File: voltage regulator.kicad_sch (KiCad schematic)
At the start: 9 parts, among them U1 AP63200WU-7

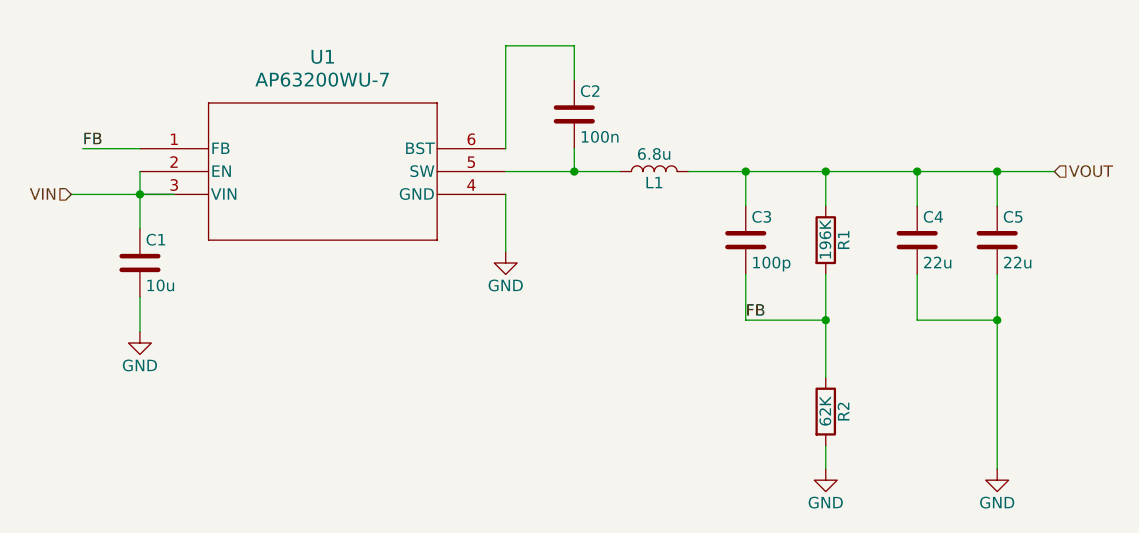
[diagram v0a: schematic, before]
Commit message: Add oscillator, mounting holes, switches
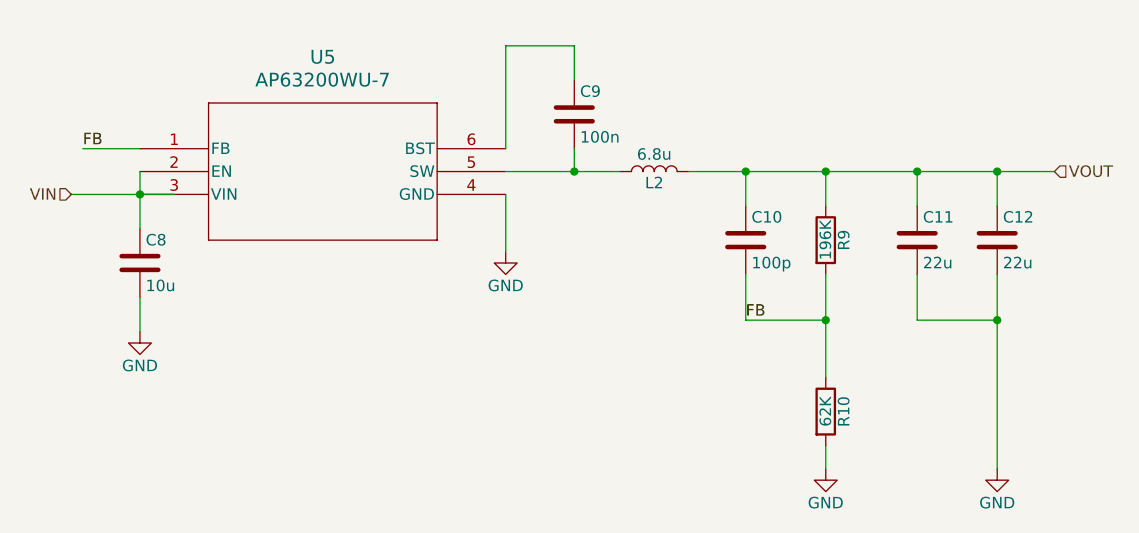
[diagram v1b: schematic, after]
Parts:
- C10: renamed from C3; footprint (none) -> Capacitor_SMD:C_0201_0603Metric_Pad0.64x0.40mm_HandSolder
- C11: renamed from C4; footprint (none) -> Capacitor_SMD:C_0201_0603Metric_Pad0.64x0.40mm_HandSolder
- C12: renamed from C5; footprint (none) -> Capacitor_SMD:C_0201_0603Metric_Pad0.64x0.40mm_HandSolder
- C8: renamed from C1; footprint (none) -> Capacitor_SMD:C_0201_0603Metric_Pad0.64x0.40mm_HandSolder
- C9: renamed from C2; footprint (none) -> Capacitor_SMD:C_0201_0603Metric_Pad0.64x0.40mm_HandSolder
- L2: renamed from L1; footprint (none) -> Inductor_SMD:L_0603_1608Metric_Pad1.05x0.95mm_HandSolder
- R10: renamed from R2; footprint (none) -> Resistor_SMD:R_0603_1608Metric_Pad0.98x0.95mm_HandSolder
- R9: renamed from R1; footprint (none) -> Resistor_SMD:R_0603_1608Metric_Pad0.98x0.95mm_HandSolder
- renumbered U1 to U5
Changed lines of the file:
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@@
 		(on_board yes)
 		(dnp no)
-		(property "Reference" "C1"
+		(property "Reference" "C8"
 			(at 100.965 95.25 0)
 			(effects
@@
 			)
 		)
-		(property "Footprint" ""
+		(property "Footprint" "Capacitor_SMD:C_0201_0603Metric_Pad0.64x0.40mm_HandSolder"
 			(at 101.2952 101.6 0)
 			(effects
@@
 		(instances
 			(project "pitch shifter"
-				(path "/155ecfb0-8543-4b20-91a8-ba83977b0554/d343d846-0f09-4042-8be7-83c2141e6a90"
-					(reference "C1")
+				(path "/155ecfb0-8543-4b20-91a8-ba83977b0554/04f7cbcd-02ba-401a-9ce7-de3392119ba4"
+					(reference "C8")
 					(unit 1)
 				)
@@
 		(on_board yes)
 		(dnp no)
-		(property "Reference" "U1"
+		(property "Reference" "U5"
 			(at 120.65 74.93 0)
 			(effects
@@
 		)
 		(instances
-			(project ""
-				(path "/155ecfb0-8543-4b20-91a8-ba83977b0554/d343d846-0f09-4042-8be7-83c2141e6a90"
-					(reference "U1")
+			(project "pitch shifter"
+				(path "/155ecfb0-8543-4b20-91a8-ba83977b0554/04f7cbcd-02ba-401a-9ce7-de3392119ba4"
+					(reference "U5")
 					(unit 1)
 				)
@@
 		(on_board yes)
 		(dnp no)
-		(property "Reference" "#PWR?"
+		(property "Reference" "#PWR014"
 			(at 195.58 127 0)
 			(effects
@@
 		(instances
 			(project "pitch shifter"
-				(path "/155ecfb0-8543-4b20-91a8-ba83977b0554/d343d846-0f09-4042-8be7-83c2141e6a90"
-					(reference "#PWR?")
+				(path "/155ecfb0-8543-4b20-91a8-ba83977b0554/04f7cbcd-02ba-401a-9ce7-de3392119ba4"
+					(reference "#PWR014")
 					(unit 1)
 				)
@@
 		(on_board yes)
 		(dnp no)
-		(property "Reference" "C3"
+		(property "Reference" "C10"
 			(at 168.275 92.71 0)
 			(effects
@@
 			)
 		)
-		(property "Footprint" ""
+		(property "Footprint" "Capacitor_SMD:C_0201_0603Metric_Pad0.64x0.40mm_HandSolder"
 			(at 168.6052 99.06 0)
 			(effects
@@
 		(instances
 			(project "pitch shifter"
-				(path "/155ecfb0-8543-4b20-91a8-ba83977b0554/d343d846-0f09-4042-8be7-83c2141e6a90"
-					(reference "C3")
+				(path "/155ecfb0-8543-4b20-91a8-ba83977b0554/04f7cbcd-02ba-401a-9ce7-de3392119ba4"
+					(reference "C10")
 					(unit 1)
 				)
@@
 		(on_board yes)
 		(dnp no)
-		(property "Reference" "#PWR?"
+		(property "Reference" "#PWR011"
 			(at 100.33 111.76 0)
 			(effects
@@
 		(instances
 			(project "pitch shifter"
-				(path "/155ecfb0-8543-4b20-91a8-ba83977b0554/d343d846-0f09-4042-8be7-83c2141e6a90"
-					(reference "#PWR?")
+				(path "/155ecfb0-8543-4b20-91a8-ba83977b0554/04f7cbcd-02ba-401a-9ce7-de3392119ba4"
+					(reference "#PWR011")
 					(unit 1)
 				)
@@
 		(on_board yes)
 		(dnp no)
-		(property "Reference" "C5"
+		(property "Reference" "C12"
 			(at 196.215 92.71 0)
 			(effects
@@
 			)
 		)
-		(property "Footprint" ""
+		(property "Footprint" "Capacitor_SMD:C_0201_0603Metric_Pad0.64x0.40mm_HandSolder"
 			(at 196.5452 99.06 0)
 			(effects
@@
 		(instances
 			(project "pitch shifter"
-				(path "/155ecfb0-8543-4b20-91a8-ba83977b0554/d343d846-0f09-4042-8be7-83c2141e6a90"
-					(reference "C5")
+				(path "/155ecfb0-8543-4b20-91a8-ba83977b0554/04f7cbcd-02ba-401a-9ce7-de3392119ba4"
+					(reference "C12")
 					(unit 1)
 				)
@@
 		(on_board yes)
 		(dnp no)
-		(property "Reference" "R1"
+		(property "Reference" "R9"
 			(at 178.562 95.25 90)
 			(effects
@@
 			)
 		)
-		(property "Footprint" ""
+		(property "Footprint" "Resistor_SMD:R_0603_1608Metric_Pad0.98x0.95mm_HandSolder"
 			(at 174.752 95.25 90)
 			(effects
@@
 		)
 		(instances
-			(project ""
-				(path "/155ecfb0-8543-4b20-91a8-ba83977b0554/d343d846-0f09-4042-8be7-83c2141e6a90"
-					(reference "R1")
+			(project "pitch shifter"
+				(path "/155ecfb0-8543-4b20-91a8-ba83977b0554/04f7cbcd-02ba-401a-9ce7-de3392119ba4"
+					(reference "R9")
 					(unit 1)
 				)
@@
 		(on_board yes)
 		(dnp no)
-		(property "Reference" "L1"
+		(property "Reference" "L2"
 			(at 157.48 88.9 90)
 			(effects
@@
 			)
 		)
-		(property "Footprint" ""
+		(property "Footprint" "Inductor_SMD:L_0603_1608Metric_Pad1.05x0.95mm_HandSolder"
 			(at 157.48 87.63 0)
 			(effects
@@
 		)
 		(instances
-			(project ""
-				(path "/155ecfb0-8543-4b20-91a8-ba83977b0554/d343d846-0f09-4042-8be7-83c2141e6a90"
-					(reference "L1")
+			(project "pitch shifter"
+				(path "/155ecfb0-8543-4b20-91a8-ba83977b0554/04f7cbcd-02ba-401a-9ce7-de3392119ba4"
+					(reference "L2")
 					(unit 1)
 				)
@@
 		(on_board yes)
 		(dnp no)
-		(property "Reference" "R2"
+		(property "Reference" "R10"
 			(at 178.562 114.3 90)
 			(effects
@@
 			)
 		)
-		(property "Footprint" ""
+		(property "Footprint" "Resistor_SMD:R_0603_1608Metric_Pad0.98x0.95mm_HandSolder"
 			(at 174.752 114.3 90)
 			(effects
@@
 		(instances
 			(project "pitch shifter"
-				(path "/155ecfb0-8543-4b20-91a8-ba83977b0554/d343d846-0f09-4042-8be7-83c2141e6a90"
-					(reference "R2")
+				(path "/155ecfb0-8543-4b20-91a8-ba83977b0554/04f7cbcd-02ba-401a-9ce7-de3392119ba4"
+					(reference "R10")
 					(unit 1)
 				)
@@
 		(on_board yes)
 		(dnp no)
-		(property "Reference" "C2"
+		(property "Reference" "C9"
 			(at 149.225 78.74 0)
 			(effects
@@
 			)
 		)
-		(property "Footprint" ""
+		(property "Footprint" "Capacitor_SMD:C_0201_0603Metric_Pad0.64x0.40mm_HandSolder"
 			(at 149.5552 85.09 0)
 			(effects
@@
 		)
 		(instances
-			(project ""
-				(path "/155ecfb0-8543-4b20-91a8-ba83977b0554/d343d846-0f09-4042-8be7-83c2141e6a90"
-					(reference "C2")
+			(project "pitch shifter"
+				(path "/155ecfb0-8543-4b20-91a8-ba83977b0554/04f7cbcd-02ba-401a-9ce7-de3392119ba4"
+					(reference "C9")
 					(unit 1)
 				)
@@
 		(on_board yes)
 		(dnp no)
-		(property "Reference" "C4"
+		(property "Reference" "C11"
 			(at 187.325 92.71 0)
 			(effects
@@
 			)
 		)
-		(property "Footprint" ""
+		(property "Footprint" "Capacitor_SMD:C_0201_0603Metric_Pad0.64x0.40mm_HandSolder"
 			(at 187.6552 99.06 0)
 			(effects
@@
 		(instances
 			(project "pitch shifter"
-				(path "/155ecfb0-8543-4b20-91a8-ba83977b0554/d343d846-0f09-4042-8be7-83c2141e6a90"
-					(reference "C4")
+				(path "/155ecfb0-8543-4b20-91a8-ba83977b0554/04f7cbcd-02ba-401a-9ce7-de3392119ba4"
+					(reference "C11")
 					(unit 1)
 				)
@@
 		(on_board yes)
 		(dnp no)
-		(property "Reference" "#PWR?"
+		(property "Reference" "#PWR013"
 			(at 176.53 127 0)
 			(effects
@@
 		(instances
 			(project "pitch shifter"
-				(path "/155ecfb0-8543-4b20-91a8-ba83977b0554/d343d846-0f09-4042-8be7-83c2141e6a90"
-					(reference "#PWR?")
+				(path "/155ecfb0-8543-4b20-91a8-ba83977b0554/04f7cbcd-02ba-401a-9ce7-de3392119ba4"
+					(reference "#PWR013")
 					(unit 1)
 				)
@@
 		(on_board yes)
 		(dnp no)
-		(property "Reference" "#PWR?"
+		(property "Reference" "#PWR012"
 			(at 140.97 102.87 0)
 			(effects
@@
 		)
 		(instances
-			(project ""
-				(path "/155ecfb0-8543-4b20-91a8-ba83977b0554/d343d846-0f09-4042-8be7-83c2141e6a90"
-					(reference "#PWR?")
-					(unit 1)
-				)
+			(project "pitch shifter"
+				(path "/155ecfb0-8543-4b20-91a8-ba83977b0554/04f7cbcd-02ba-401a-9ce7-de3392119ba4"
+					(reference "#PWR012")
+					(unit 1)
+				)

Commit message: Began board layout
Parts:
- removed C10: 100p, Capacitor_SMD:C_0201_0603Metric_Pad0.64x0.40mm_HandSolder, symbol Device:C
- removed C11, C12: 22u, Capacitor_SMD:C_0201_0603Metric_Pad0.64x0.40mm_HandSolder, symbol Device:C
- removed C8: 10u, Capacitor_SMD:C_0201_0603Metric_Pad0.64x0.40mm_HandSolder, symbol Device:C
- removed C9: 100n, Capacitor_SMD:C_0201_0603Metric_Pad0.64x0.40mm_HandSolder, symbol Device:C
- removed R10: 62K, Resistor_SMD:R_0603_1608Metric_Pad0.98x0.95mm_HandSolder, symbol Device:R
- removed R9: 196K, Resistor_SMD:R_0603_1608Metric_Pad0.98x0.95mm_HandSolder, symbol Device:R
- added C15: 10u, Capacitor_SMD:C_0603_1608Metric_Pad1.08x0.95mm_HandSolder, symbol Device:C
- added C17: 100n, Capacitor_SMD:C_0603_1608Metric_Pad1.08x0.95mm_HandSolder, symbol Device:C
- added C19: 100p, Capacitor_SMD:C_0603_1608Metric_Pad1.08x0.95mm_HandSolder, symbol Device:C
- added C21, C23: 22u, Capacitor_SMD:C_0603_1608Metric_Pad1.08x0.95mm_HandSolder, symbol Device:C
- added R17: 196K, Resistor_SMD:R_0603_1608Metric_Pad0.98x0.95mm_HandSolder, symbol Device:R
- added R18: 62K, Resistor_SMD:R_0603_1608Metric_Pad0.98x0.95mm_HandSolder, symbol Device:R
- added TP35, TP36, TP37, TP38: Test Point, TestPoint:TestPoint_THTPad_D1.0mm_Drill0.5mm, symbol Project_Components:Inline Test Point
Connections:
- net FB: now also C19.2, R17.2, R18.1, TP35.1
- net GND: now also C15.2, C21.2, C23.2, R18.2
- net VIN: now also C15.1
- net VOUT: now also C19.1, C21.1, C23.1, R17.1, TP38.1
- net at L2.1, U5.5 (SW): now also C17.2, TP37.1
- net at U5.6 (BST): now also C17.1, TP36.1
